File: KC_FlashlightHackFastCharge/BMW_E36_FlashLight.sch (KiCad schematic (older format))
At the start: 12 parts, among them J1 CONN_01X01_FEMALE, J2 CONN_01X01_FEMALE, Q1 BSS138, SW1 SW_DIP_x01

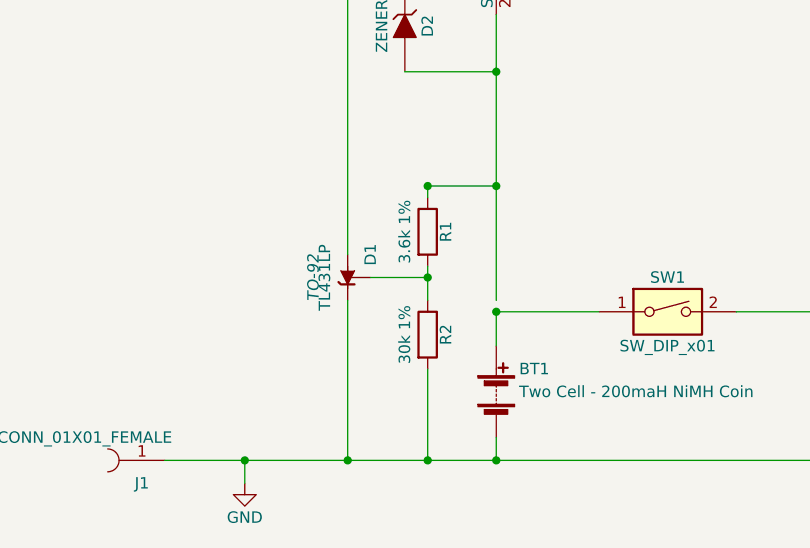
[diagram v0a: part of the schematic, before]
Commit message: Adjusted the Treshold Voltage
Changed the threshold voltage from 2.8v to 2.75v
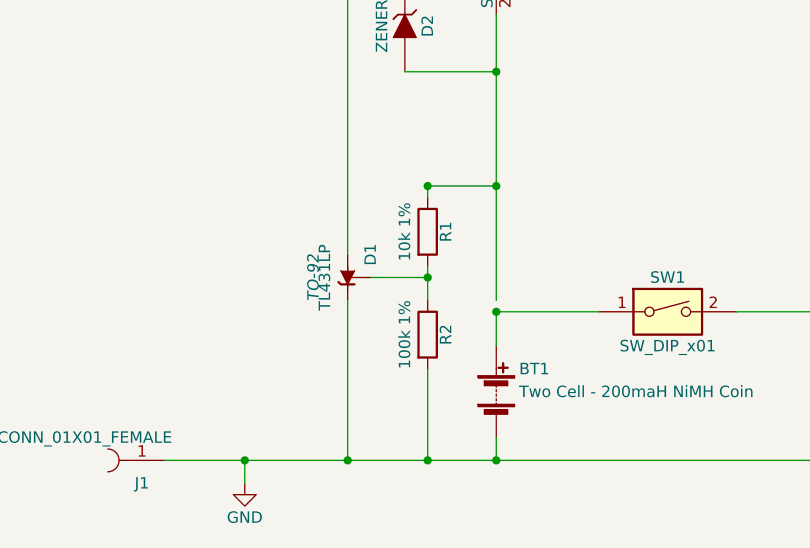
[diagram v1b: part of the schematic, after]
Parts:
- R1: value 3.6k 1% -> 10k 1%
- R2: value 30k 1% -> 100k 1%
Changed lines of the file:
@@
 P 5900 4450
 F 0 "R1" V 5980 4450 50  0000 C CNN
-F 1 "3.6k 1%" V 5800 4450 50  0000 C CNN
+F 1 "10k 1%" V 5800 4450 50  0000 C CNN
 F 2 "" V 5830 4450 50  0000 C CNN
 F 3 "" H 5900 4450 50  0000 C CNN
@@
 P 5900 4900
 F 0 "R2" V 5980 4900 50  0000 C CNN
-F 1 "30k 1%" V 5800 4900 50  0000 C CNN
+F 1 "100k 1%" V 5800 4900 50  0000 C CNN
 F 2 "" V 5830 4900 50  0000 C CNN
 F 3 "" H 5900 4900 50  0000 C CNN

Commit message: Fixed the orientation of the TL431.  The anode and cathode were reversed, but now fixed.
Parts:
- Q1: symbol BSS138 -> BSS138-RESCUE-BMW_E36_FlashLight
- SW1: symbol SW_DIP_x01 -> SW_DIP_x01-RESCUE-BMW_E36_FlashLight
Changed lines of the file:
@@
 $EndComp
 $Comp
-L SW_DIP_x01 SW1
+L SW_DIP_x01-RESCUE-BMW_E36_FlashLight SW1
 U 1 1 59781418
 P 6950 4800
@@
 F 3 "" H 5550 4650 50  0000 C CNN
 	1    5550 4650
-	0    1    1    0
+	0    1    -1   0
 $EndComp
-Wire Wire Line
-	5550 2700 5550 4550
 Connection ~ 6200 4250
-Wire Wire Line
-	5550 4750 5550 5450
 Connection ~ 5550 5450
 $Comp
@@
 $EndComp
 Wire Wire Line
-	5650 4650 5900 4650
-Wire Wire Line
 	5900 4600 5900 4750
 Connection ~ 5900 4650
@@
 Connection ~ 5900 5450
 $Comp
-L BSS138 Q1
+L BSS138-RESCUE-BMW_E36_FlashLight Q1
 U 1 1 5978259C
 P 6100 3300
@@
 Wire Wire Line
 	6200 4950 6200 4800
+Wire Wire Line
+	5650 4650 5900 4650
+Wire Wire Line
+	5550 4750 5550 5450
+Wire Wire Line
+	5550 2700 5550 4550
 $EndSCHEMATC
